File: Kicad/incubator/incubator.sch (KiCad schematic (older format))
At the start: 15 parts, among them J1 Barrel_Jack_MountingPin, J3 Conn_02x03_Odd_Even, J4 RJ12, J5 Conn_01x05

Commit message: refactor: Kicad design updated
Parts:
- removed D1: MBR0520LT, Diode_SMD:D_SOD-123, symbol Diode:MBR0520LT
- removed J3: Conn_02x03_Odd_Even, Connector:Tag-Connect_TC2030-IDC-NL_2x03_P1.27mm_Vertical, symbol Connector_Generic:Conn_02x03_Odd_Even
- added C7: 100n, Capacitor_SMD:C_0805_2012Metric_Pad1.18x1.45mm_HandSolder, symbol Device:C
- added D4, D5: MBR0520LT, Diode_SMD:D_SOD-123, symbol Diode:MBR0520LT
- added J2: Conn_01x06, Connector_PinHeader_2.54mm:PinHeader_1x06_P2.54mm_Vertical, symbol Connector_Generic:Conn_01x06
- H5, H6, H7, H8: footprint MountingHole:MountingHole_3.2mm_M3 -> MountingHole:MountingHole_4.5mm
- J1: symbol incubator:Barrel_Jack_MountingPin -> incubator-rescue:Barrel_Jack_MountingPin-incubator
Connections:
- net labels added: RX, TX
- net labels removed: D1, ONE-WIRE
- wire segments 79 -> 84
- no-connect marks 2 -> 3
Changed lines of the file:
@@
 	1    0    0    -1
 $EndComp
-Text GLabel 4975 3875 0    50   Input ~ 0
+Text GLabel 4975 3850 0    50   Input ~ 0
 12V
-Wire Wire Line
-	5150 3875 5075 3875
-Wire Wire Line
-	5075 3875 5075 3800
 $Comp
 L power:GND #PWR0102
@@
 F 0 "H5" H 5125 7271 50  0000 L CNN
 F 1 "MountingHole" H 5125 7180 50  0000 L CNN
-F 2 "MountingHole:MountingHole_3.2mm_M3" H 5025 7225 50  0001 C CNN
+F 2 "MountingHole:MountingHole_4.5mm" H 5025 7225 50  0001 C CNN
 F 3 "~" H 5025 7225 50  0001 C CNN
 	1    5025 7225
@@
 F 0 "H7" H 5900 7271 50  0000 L CNN
 F 1 "MountingHole" H 5900 7180 50  0000 L CNN
-F 2 "MountingHole:MountingHole_3.2mm_M3" H 5800 7225 50  0001 C CNN
+F 2 "MountingHole:MountingHole_4.5mm" H 5800 7225 50  0001 C CNN
 F 3 "~" H 5800 7225 50  0001 C CNN
 	1    5800 7225
@@
 F 0 "H6" H 5125 7546 50  0000 L CNN
 F 1 "MountingHole" H 5125 7455 50  0000 L CNN
-F 2 "MountingHole:MountingHole_3.2mm_M3" H 5025 7500 50  0001 C CNN
+F 2 "MountingHole:MountingHole_4.5mm" H 5025 7500 50  0001 C CNN
 F 3 "~" H 5025 7500 50  0001 C CNN
 	1    5025 7500
@@
 F 0 "H8" H 5900 7521 50  0000 L CNN
 F 1 "MountingHole" H 5900 7430 50  0000 L CNN
-F 2 "MountingHole:MountingHole_3.2mm_M3" H 5800 7475 50  0001 C CNN
+F 2 "MountingHole:MountingHole_4.5mm" H 5800 7475 50  0001 C CNN
 F 3 "~" H 5800 7475 50  0001 C CNN
 	1    5800 7475
 	1    0    0    -1
 $EndComp
-$Comp
-L power:+12V #PWR0103
-U 1 1 6111A394
-P 5075 3800
-F 0 "#PWR0103" H 5075 3650 50  0001 C CNN
-F 1 "+12V" H 5090 3973 50  0000 C CNN
-F 2 "" H 5075 3800 50  0001 C CNN
-F 3 "" H 5075 3800 50  0001 C CNN
-	1    5075 3800
-	1    0    0    -1
-$EndComp
-Wire Wire Line
-	4975 3875 5075 3875
-Connection ~ 5075 3875
 $Comp
 L power:+12V #PWR0104
@@
 	2700 925  2700 775
 Wire Wire Line
-	1725 3025 1725 3075
-Wire Wire Line
-	1675 3025 1725 3025
-$Comp
-L power:GND #PWR0107
-U 1 1 610302A6
-P 1725 3075
-F 0 "#PWR0107" H 1725 2825 50  0001 C CNN
-F 1 "GND" H 1730 2902 50  0000 C CNN
-F 2 "" H 1725 3075 50  0001 C CNN
-F 3 "" H 1725 3075 50  0001 C CNN
-	1    1725 3075
-	1    0    0    -1
-$EndComp
-Wire Wire Line
-	1675 2925 1750 2925
-Wire Wire Line
-	1075 3025 1175 3025
-Wire Wire Line
-	1175 2925 1075 2925
-Wire Wire Line
-	1075 2825 1175 2825
-Text GLabel 1750 2925 2    50   Input ~ 0
-MOSI
-Text GLabel 1075 3025 0    50   Input ~ 0
-~RESET
-Text GLabel 1075 2925 0    50   Input ~ 0
-SCK
-Text GLabel 1075 2825 0    50   Input ~ 0
-MISO
-$Comp
-L Connector_Generic:Conn_02x03_Odd_Even J3
-U 1 1 6104194C
-P 1375 2925
-F 0 "J3" H 1250 2750 50  0000 C CNN
-F 1 "Conn_02x03_Odd_Even" H 1175 2675 50  0000 C CNN
-F 2 "Connector:Tag-Connect_TC2030-IDC-NL_2x03_P1.27mm_Vertical" H 1375 2925 50  0001 C CNN
-F 3 "~" H 1375 2925 50  0001 C CNN
-	1    1375 2925
-	1    0    0    -1
-$EndComp
-Wire Wire Line
-	2675 1975 2775 1975
+	1625 1925 1725 1925
 $Sheet
-S 1875 1700 800  575
+S 825  1650 800  575
 U 61054A11
 F0 "Sheet 5 V Step-down" 50
 F1 "5.sch" 50
-F2 "VIN" I L 1875 1925 50
-F3 "GND" I L 1875 2050 50
-F4 "5V" I R 2675 1975 50
+F2 "VIN" I L 825 1875 50
+F3 "GND" I L 825 2000 50
+F4 "5V" I R 1625 1925 50
 $EndSheet
-Text GLabel 2775 1975 2    50   Input ~ 0
-VIN
-Wire Wire Line
-	1775 2050 1775 2100
-Wire Wire Line
-	1875 2050 1775 2050
+Wire Wire Line
+	725  2000 725  2050
+Wire Wire Line
+	825  2000 725  2000
 $Comp
 L power:GND #PWR0109
 U 1 1 61068D10
-P 1775 2100
-F 0 "#PWR0109" H 1775 1850 50  0001 C CNN
-F 1 "GND" H 1780 1927 50  0000 C CNN
-F 2 "" H 1775 2100 50  0001 C CNN
-F 3 "" H 1775 2100 50  0001 C CNN
-	1    1775 2100
-	1    0    0    -1
-$EndComp
-Wire Wire Line
-	1875 1925 1775 1925
-Text GLabel 1775 1925 0    50   Input ~ 0
+P 725 2050
+F 0 "#PWR0109" H 725 1800 50  0001 C CNN
+F 1 "GND" H 730 1877 50  0000 C CNN
+F 2 "" H 725 2050 50  0001 C CNN
+F 3 "" H 725 2050 50  0001 C CNN
+	1    725  2050
+	1    0    0    -1
+$EndComp
+Wire Wire Line
+	825  1875 725  1875
+Text GLabel 725  1875 0    50   Input ~ 0
 12V
 Wire Wire Line
@@
 	1650 1025 1650 1100
 NoConn ~ 1275 1225
-$Comp
-L Diode:MBR0520LT D1
-U 1 1 613041E6
-P 2050 2825
-F 0 "D1" H 2050 2608 50  0000 C CNN
-F 1 "MBR0520LT" H 2050 2699 50  0000 C CNN
-F 2 "Diode_SMD:D_SOD-123" H 2050 2650 50  0001 C CNN
-F 3 "http://www.onsemi.com/pub_link/Collateral/MBR0520LT1-D.PDF" H 2050 2825 50  0001 C CNN
-	1    2050 2825
-	-1   0    0    1
-$EndComp
-Wire Wire Line
-	1675 2825 1900 2825
-Text GLabel 2275 2825 2    50   Input ~ 0
-VIN
-Wire Wire Line
-	2200 2825 2275 2825
 Wire Notes Line
 	3000 475  3000 4850
@@
 Wire Notes Line
 	5925 475  5925 6550
-Text Notes 625  2150 0    150  ~ 0
+Text Notes 2100 1600 0    150  ~ 0
 Power\nSupply
 Text Notes 2000 3675 0    150  ~ 0
@@
 D2
 Text GLabel 5025 2225 2    50   Input ~ 0
-D1
+TX
 Text GLabel 5025 2125 2    50   Input ~ 0
-ONE-WIRE
+RX
 Text GLabel 3900 1025 0    50   Input ~ 0
 VIN
@@
 	3900 2825 3900 2950
 Text GLabel 6250 1325 0    50   Input ~ 0
-D1
+C3
 Text GLabel 6250 1650 0    50   Input ~ 0
+C1
+Text GLabel 6250 1750 0    50   Input ~ 0
+C0
+Text GLabel 7025 1325 2    50   Input ~ 0
+C2
+Text GLabel 7025 1425 2    50   Input ~ 0
 D2
-Text GLabel 6250 1750 0    50   Input ~ 0
+Text GLabel 7025 1525 2    50   Input ~ 0
 D3
-Text GLabel 7025 1325 2    50   Input ~ 0
+Text GLabel 7025 1625 2    50   Input ~ 0
 D4
-Text GLabel 7025 1425 2    50   Input ~ 0
+Text GLabel 7025 1775 2    50   Input ~ 0
 D5
-Text GLabel 7025 1525 2    50   Input ~ 0
+Text GLabel 7025 1875 2    50   Input ~ 0
 D6
-Text GLabel 7025 1625 2    50   Input ~ 0
+Text GLabel 7025 1975 2    50   Input ~ 0
 D7
-Text GLabel 7025 1775 2    50   Input ~ 0
-C0
-Text GLabel 7025 1875 2    50   Input ~ 0
-C1
-Text GLabel 7025 1975 2    50   Input ~ 0
-C2
 $Comp
 L power:GND #PWR0114
@@
 	475  3325 5925 3325
 $Comp
-L incubator:Barrel_Jack_MountingPin J1
+L incubator-rescue:Barrel_Jack_MountingPin-incubator J1
 U 1 1 61123504
 P 1275 925
 F 0 "J1" H 1332 1242 50  0000 C CNN
-F 1 "Barrel_Jack_MountingPin" H 1332 1151 50  0000 C CNN
+F 1 "Barrel_Jack_MountingPin" H 1100 1150 50  0000 C CNN
 F 2 "Connector_BarrelJack:BarrelJack_Horizontal" H 1325 885 50  0001 C CNN
 F 3 "~" H 1325 885 50  0001 C CNN
@@
 	1    0    0    -1
 $EndComp
+$Comp
+L Connector_Generic:Conn_01x06 J2
+U 1 1 610D151B
+P 7600 3675
+F 0 "J2" H 7680 3667 50  0000 L CNN
+F 1 "Conn_01x06" H 7425 3275 50  0000 L CNN
+F 2 "Connector_PinHeader_2.54mm:PinHeader_1x06_P2.54mm_Vertical" H 7600 3675 50  0001 C CNN
+F 3 "~" H 7600 3675 50  0001 C CNN
+	1    7600 3675
+	1    0    0    -1
+$EndComp
+Text GLabel 2100 1925 2    50   Input ~ 0
+VIN
+Text GLabel 4975 3950 0    50   Input ~ 0
+VIN
+Wire Wire Line
+	4975 3950 5150 3950
+Text GLabel 8050 3325 2    50   Input ~ 0
+~RESET
+Text GLabel 7275 3575 0    50   Input ~ 0
+TX
+$Comp
+L power:GND #PWR0103
+U 1 1 610EBE3F
+P 7325 4050
+F 0 "#PWR0103" H 7325 3800 50  0001 C CNN
+F 1 "GND" H 7330 3877 50  0000 C CNN
+F 2 "" H 7325 4050 50  0001 C CNN
+F 3 "" H 7325 4050 50  0001 C CNN
+	1    7325 4050
+	1    0    0    -1
+$EndComp
+Wire Wire Line
+	7400 3575 7275 3575
+Wire Wire Line
+	7275 3675 7400 3675
+Wire Wire Line
+	7400 3975 7325 3975
+Wire Wire Line
+	7325 3975 7325 4050
+Text GLabel 7275 3675 0    50   Input ~ 0
+RX
+$Comp
+L Diode:MBR0520LT D4
+U 1 1 61137931
+P 1875 1925
+F 0 "D4" H 1875 1708 50  0000 C CNN
+F 1 "MBR0520LT" H 1875 1799 50  0000 C CNN
+F 2 "Diode_SMD:D_SOD-123" H 1875 1750 50  0001 C CNN
+F 3 "http://www.onsemi.com/pub_link/Collateral/MBR0520LT1-D.PDF" H 1875 1925 50  0001 C CNN
+	1    1875 1925
+	-1   0    0    1
+$EndComp
+Wire Wire Line
+	2100 1925 2025 1925
+$Comp
+L Device:C C?
+U 1 1 61154027
+P 7900 3525
+AR Path="/61116939/61154027" Ref="C?"  Part="1"
+AR Path="/61154027" Ref="C7"  Part="1"
+F 0 "C7" H 8015 3571 50  0000 L CNN
+F 1 "100n" H 8015 3480 50  0000 L CNN
+F 2 "Capacitor_SMD:C_0805_2012Metric_Pad1.18x1.45mm_HandSolder" H 7938 3375 50  0001 C CNN
+F 3 "~" H 7900 3525 50  0001 C CNN
+	1    7900 3525
+	1    0    0    -1
+$EndComp
+Wire Wire Line
+	7100 3775 7400 3775
+Wire Wire Line
+	6800 3775 6700 3775
+Text GLabel 6700 3775 0    50   Input ~ 0
+VIN
+Wire Wire Line
+	7400 3475 7325 3475
+Wire Wire Line
+	7325 3475 7325 3325
+Wire Wire Line
+	7325 3325 7900 3325
+$Comp
+L power:GND #PWR0106
+U 1 1 6117A969
+P 7900 3775
+F 0 "#PWR0106" H 7900 3525 50  0001 C CNN
+F 1 "GND" H 7905 3602 50  0000 C CNN
+F 2 "" H 7900 3775 50  0001 C CNN
+F 3 "" H 7900 3775 50  0001 C CNN
+	1    7900 3775
+	1    0    0    -1
+$EndComp
+Wire Wire Line
+	7900 3775 7900 3675
+Wire Wire Line
+	7900 3375 7900 3325
+Connection ~ 7900 3325
+Wire Wire Line
+	7900 3325 8050 3325
+Text GLabel 1725 825  2    50   Input ~ 0
+12V
+Wire Wire Line
+	1725 825  1650 825
+Connection ~ 1650 825
+Wire Wire Line
+	4975 3850 5150 3850
+$Comp
+L Diode:MBR0520LT D5
+U 1 1 61109529
+P 6950 3775
+F 0 "D5" H 6950 3558 50  0000 C CNN
+F 1 "MBR0520LT" H 6800 3650 50  0000 C CNN
+F 2 "Diode_SMD:D_SOD-123" H 6950 3600 50  0001 C CNN
+F 3 "http://www.onsemi.com/pub_link/Collateral/MBR0520LT1-D.PDF" H 6950 3775 50  0001 C CNN
+	1    6950 3775
+	1    0    0    -1
+$EndComp
+NoConn ~ 7400 3875
 $EndSCHEMATC

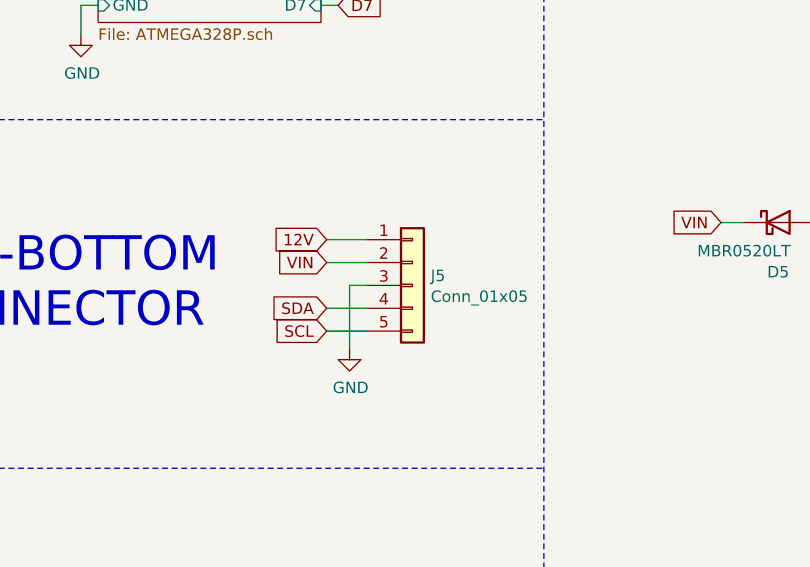
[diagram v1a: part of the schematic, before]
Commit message: fix: change top-bottom connector for individual pad
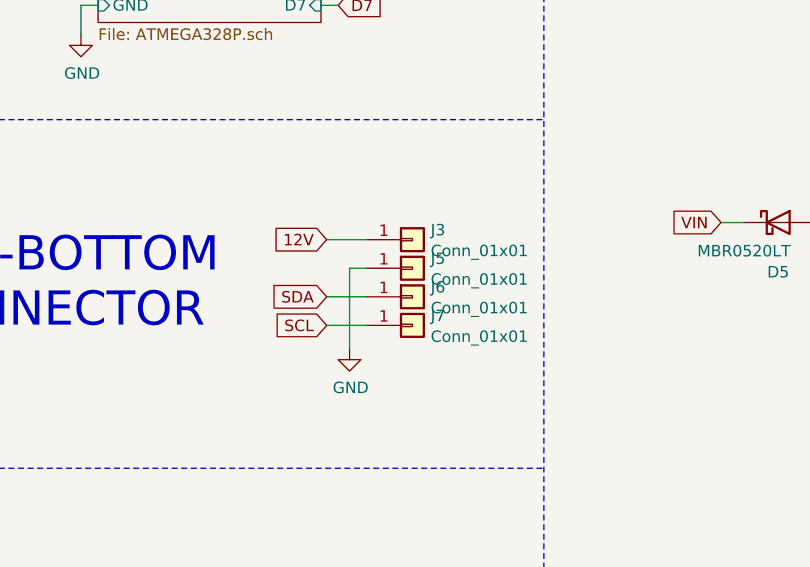
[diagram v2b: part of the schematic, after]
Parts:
- removed J5: Conn_01x05, Connector_Molex:Molex_KK-254_AE-6410-05A_1x05_P2.54mm_Vertical, symbol Connector_Generic:Conn_01x05
- added J3, J5, J6, J7: Conn_01x01, Connector_Wire:SolderWirePad_1x01_SMD_5x10mm, symbol Connector_Generic:Conn_01x01
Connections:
- net +12V: now also J3.1 (Pin_1)
- net GND: now also J5.1 (Pin_1)
- net SCL: now also J7.1 (Pin_1)
- net SDA: now also J6.1 (Pin_1)
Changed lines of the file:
@@
 $EndComp
 Wire Wire Line
-	5150 4050 5075 4050
-Wire Wire Line
-	5075 4050 5075 4325
-Text GLabel 4975 4150 0    50   Input ~ 0
+	5150 3975 5075 3975
+Wire Wire Line
+	5075 3975 5075 4325
+Text GLabel 4975 4100 0    50   Input ~ 0
 SDA
-Text GLabel 4975 4250 0    50   Input ~ 0
+Text GLabel 4975 4225 0    50   Input ~ 0
 SCL
 Wire Wire Line
-	5150 4250 4975 4250
-Wire Wire Line
-	4975 4150 5150 4150
+	5150 4225 4975 4225
+Wire Wire Line
+	4975 4100 5150 4100
 $Comp
 L Mechanical:MountingHole H5
@@
 Text Notes 4675 6850 0    102  ~ 0
 HOLES
-$Comp
-L Connector_Generic:Conn_01x05 J5
-U 1 1 6118C3B2
-P 5350 4050
-F 0 "J5" H 5430 4092 50  0000 L CNN
-F 1 "Conn_01x05" H 5430 4001 50  0000 L CNN
-F 2 "Connector_Molex:Molex_KK-254_AE-6410-05A_1x05_P2.54mm_Vertical" H 5350 4050 50  0001 C CNN
-F 3 "~" H 5350 4050 50  0001 C CNN
-	1    5350 4050
-	1    0    0    -1
-$EndComp
 Wire Wire Line
 	5025 1675 4950 1675
@@
 Text GLabel 2100 1925 2    50   Input ~ 0
 VIN
-Text GLabel 4975 3950 0    50   Input ~ 0
-VIN
-Wire Wire Line
-	4975 3950 5150 3950
 Text GLabel 8050 3325 2    50   Input ~ 0
 ~RESET
@@
 $EndComp
 NoConn ~ 7400 3875
+$Comp
+L Connector_Generic:Conn_01x01 J3
+U 1 1 6124B8B1
+P 5350 3850
+F 0 "J3" H 5430 3892 50  0000 L CNN
+F 1 "Conn_01x01" H 5430 3801 50  0000 L CNN
+F 2 "Connector_Wire:SolderWirePad_1x01_SMD_5x10mm" H 5350 3850 50  0001 C CNN
+F 3 "~" H 5350 3850 50  0001 C CNN
+	1    5350 3850
+	1    0    0    -1
+$EndComp
+$Comp
+L Connector_Generic:Conn_01x01 J5
+U 1 1 61251C91
+P 5350 3975
+F 0 "J5" H 5430 4017 50  0000 L CNN
+F 1 "Conn_01x01" H 5430 3926 50  0000 L CNN
+F 2 "Connector_Wire:SolderWirePad_1x01_SMD_5x10mm" H 5350 3975 50  0001 C CNN
+F 3 "~" H 5350 3975 50  0001 C CNN
+	1    5350 3975
+	1    0    0    -1
+$EndComp
+$Comp
+L Connector_Generic:Conn_01x01 J6
+U 1 1 61252053
+P 5350 4100
+F 0 "J6" H 5430 4142 50  0000 L CNN
+F 1 "Conn_01x01" H 5430 4051 50  0000 L CNN
+F 2 "Connector_Wire:SolderWirePad_1x01_SMD_5x10mm" H 5350 4100 50  0001 C CNN
+F 3 "~" H 5350 4100 50  0001 C CNN
+	1    5350 4100
+	1    0    0    -1
+$EndComp
+$Comp
+L Connector_Generic:Conn_01x01 J7
+U 1 1 61252475
+P 5350 4225
+F 0 "J7" H 5430 4267 50  0000 L CNN
+F 1 "Conn_01x01" H 5430 4176 50  0000 L CNN
+F 2 "Connector_Wire:SolderWirePad_1x01_SMD_5x10mm" H 5350 4225 50  0001 C CNN
+F 3 "~" H 5350 4225 50  0001 C CNN
+	1    5350 4225
+	1    0    0    -1
+$EndComp
 $EndSCHEMATC

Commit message: fix: fan size and push button position
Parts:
- C7: symbol Device:C -> incubator-rescue:C-Device
- D4, D5: symbol Diode:MBR0520LT -> incubator-rescue:MBR0520LT-Diode
- H1, H2, H3, H4, H5, H6, H7, H8: symbol Mechanical:MountingHole -> incubator-rescue:MountingHole-Mechanical
- J2: symbol Connector_Generic:Conn_01x06 -> incubator-rescue:Conn_01x06-Connector_Generic
- J3, J5, J6, J7: symbol Connector_Generic:Conn_01x01 -> incubator-rescue:Conn_01x01-Connector_Generic
- J4: symbol Connector:RJ12 -> incubator-rescue:RJ12-Connector
- R1, R2: symbol Device:R -> incubator-rescue:R-Device
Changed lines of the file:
@@
 $EndDescr
 $Comp
-L power:VCC #PWR0101
+L incubator-rescue:VCC-power #PWR0101
 U 1 1 610EABF4
 P 2200 925
@@
 $EndComp
 $Comp
-L power:PWR_FLAG #FLG0101
+L incubator-rescue:PWR_FLAG-power #FLG0101
 U 1 1 610EC89D
 P 2200 775
@@
 	2200 775  2200 925
 $Comp
-L Mechanical:MountingHole H1
+L incubator-rescue:MountingHole-Mechanical H1
 U 1 1 610F54D5
 P 3325 7175
@@
 $EndComp
 $Comp
-L Mechanical:MountingHole H3
+L incubator-rescue:MountingHole-Mechanical H3
 U 1 1 610F73E9
 P 4100 7175
@@
 $EndComp
 $Comp
-L Mechanical:MountingHole H2
+L incubator-rescue:MountingHole-Mechanical H2
 U 1 1 610F770E
 P 3325 7475
@@
 $EndComp
 $Comp
-L Mechanical:MountingHole H4
+L incubator-rescue:MountingHole-Mechanical H4
 U 1 1 610F79C8
 P 4100 7475
@@
 12V
 $Comp
-L power:GND #PWR0102
+L incubator-rescue:GND-power #PWR0102
 U 1 1 611DACB0
 P 5075 4325
@@
 	4975 4100 5150 4100
 $Comp
-L Mechanical:MountingHole H5
+L incubator-rescue:MountingHole-Mechanical H5
 U 1 1 6110AD0D
 P 5025 7225
@@
 $EndComp
 $Comp
-L Mechanical:MountingHole H7
+L incubator-rescue:MountingHole-Mechanical H7
 U 1 1 6110B26F
 P 5800 7225
@@
 $EndComp
 $Comp
-L Mechanical:MountingHole H6
+L incubator-rescue:MountingHole-Mechanical H6
 U 1 1 6110B9C7
 P 5025 7500
@@
 $EndComp
 $Comp
-L Mechanical:MountingHole H8
+L incubator-rescue:MountingHole-Mechanical H8
 U 1 1 6110BE5B
 P 5800 7475
@@
 $EndComp
 $Comp
-L power:+12V #PWR0104
+L incubator-rescue:+12V-power #PWR0104
 U 1 1 61121502
 P 2700 925
@@
 $EndComp
 $Comp
-L power:PWR_FLAG #FLG0102
+L incubator-rescue:PWR_FLAG-power #FLG0102
 U 1 1 611229BC
 P 2700 775
@@
 	825  2000 725  2000
 $Comp
-L power:GND #PWR0109
+L incubator-rescue:GND-power #PWR0109
 U 1 1 61068D10
 P 725 2050
@@
 	1425 3725 1425 3675
 $Comp
-L power:VCC #PWR0110
+L incubator-rescue:VCC-power #PWR0110
 U 1 1 610EC2F5
 P 1150 3625
@@
 NoConn ~ 1700 4400
 $Comp
-L power:GND #PWR0111
+L incubator-rescue:GND-power #PWR0111
 U 1 1 610DD35E
 P 1625 4575
@@
 	1700 4000 1650 4000
 $Comp
-L Device:R R1
+L incubator-rescue:R-Device R1
 U 1 1 610DC2A0
 P 1150 3875
@@
 $EndComp
 $Comp
-L Device:R R2
+L incubator-rescue:R-Device R2
 U 1 1 610DBA03
 P 1425 3875
@@
 12V
 $Comp
-L Connector:RJ12 J4
+L incubator-rescue:RJ12-Connector J4
 U 1 1 610CF354
 P 2100 4200
@@
 $EndComp
 $Comp
-L power:+12V #PWR0112
+L incubator-rescue:+12V-power #PWR0112
 U 1 1 61248C9C
 P 1650 750
@@
 $EndComp
 $Comp
-L power:GND #PWR0113
+L incubator-rescue:GND-power #PWR0113
 U 1 1 6124A445
 P 1650 1100
@@
 ~RESET
 $Comp
-L power:GND #PWR0105
+L incubator-rescue:GND-power #PWR0105
 U 1 1 6100E2AC
 P 3900 2950
@@
 D4
 Text GLabel 7025 1775 2    50   Input ~ 0
+D6
+Text GLabel 7025 1875 2    50   Input ~ 0
 D5
-Text GLabel 7025 1875 2    50   Input ~ 0
-D6
 Text GLabel 7025 1975 2    50   Input ~ 0
 D7
 $Comp
-L power:GND #PWR0114
+L incubator-rescue:GND-power #PWR0114
 U 1 1 611DEBA3
 P 6300 2075
@@
 $EndComp
 $Comp
-L Connector_Generic:Conn_01x06 J2
+L incubator-rescue:Conn_01x06-Connector_Generic J2
 U 1 1 610D151B
 P 7600 3675
@@
 TX
 $Comp
-L power:GND #PWR0103
+L incubator-rescue:GND-power #PWR0103
 U 1 1 610EBE3F
 P 7325 4050
@@
 RX
 $Comp
-L Diode:MBR0520LT D4
+L incubator-rescue:MBR0520LT-Diode D4
 U 1 1 61137931
 P 1875 1925
@@
 	2100 1925 2025 1925
 $Comp
-L Device:C C?
+L incubator-rescue:C-Device C?
 U 1 1 61154027
 P 7900 3525
@@
 	7325 3325 7900 3325
 $Comp
-L power:GND #PWR0106
+L incubator-rescue:GND-power #PWR0106
 U 1 1 6117A969
 P 7900 3775
@@
 	4975 3850 5150 3850
 $Comp
-L Diode:MBR0520LT D5
+L incubator-rescue:MBR0520LT-Diode D5
 U 1 1 61109529
 P 6950 3775
@@
 NoConn ~ 7400 3875
 $Comp
-L Connector_Generic:Conn_01x01 J3
+L incubator-rescue:Conn_01x01-Connector_Generic J3
 U 1 1 6124B8B1
 P 5350 3850
@@
 $EndComp
 $Comp
-L Connector_Generic:Conn_01x01 J5
+L incubator-rescue:Conn_01x01-Connector_Generic J5
 U 1 1 61251C91
 P 5350 3975
@@
 $EndComp
 $Comp
-L Connector_Generic:Conn_01x01 J6
+L incubator-rescue:Conn_01x01-Connector_Generic J6
 U 1 1 61252053
 P 5350 4100
@@
 $EndComp
 $Comp
-L Connector_Generic:Conn_01x01 J7
+L incubator-rescue:Conn_01x01-Connector_Generic J7
 U 1 1 61252475
 P 5350 4225
